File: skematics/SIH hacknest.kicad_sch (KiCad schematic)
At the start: 20 parts, among them J1 Screw_Terminal_01x02, J10 Conn_2Rows-05Pins, J11 oled 1.3inch, J12 oled 0.96inch, J13 Conn_2Rows-05Pins, J14 Conn_2Rows-05Pins, J2 Screw_Terminal_01x02, J3 MQ137, J4 LOADCELL FLOCK, J5 LOAD CELL FEED, J6 BH1750, J7 Conn_2Rows-05Pins, J8 Conn_2Rows-05Pins, J9 Conn_2Rows-05Pins, SW1 SW_SPDT, U1 DHT22, U2 ESP32-S2-WROVER, U3 HX711, U4 BUCK CONVERTER

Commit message: updated sch
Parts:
- added J15: FLOW SENSOR, symbol Connector:Conn_01x03_Pin
- added J16: COMMON RAIL +VE, symbol Connector_Generic:Conn_2Rows-05Pins
- added J17: COMMON RAIL -VE, symbol Connector_Generic:Conn_2Rows-05Pins
- added J18: max9812 MIC, symbol Connector:Conn_01x03_Pin
- added K1: RELAY GENRAL-1, Relay_THT:Relay_StandexMeder_DIP_LowProfile, symbol Relay:DIPxx-1Axx-12x
- added K2: RELAY GENERAL 2, Relay_THT:Relay_StandexMeder_DIP_LowProfile, symbol Relay:DIPxx-1Axx-12x
- added SW2, SW3, SW4, SW5: SW_Push, symbol Switch:SW_Push
- J10, J8: value Conn_2Rows-05Pins -> COMMON RAIL -VE
- J13: value Conn_2Rows-05Pins -> COMMON SDA
- J14: value Conn_2Rows-05Pins -> COMMON SCA
- J7, J9: value Conn_2Rows-05Pins -> COMMON RAIL +VE
- U2: value ESP32-S2-WROVER -> ESP32-WROVER
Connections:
- net at J11.1 (vcc), J12.1 (vcc): now also J15.1 (Pin_1), J16.5 (Pin_5), J18.1 (Pin_1)
- net at J11.2 (gnd), J12.2 (gnd): now also J15.2 (Pin_2), J17.1 (Pin_1), J18.2 (Pin_2)
- net at J9.2 (Pin_2): now also J4.2 (Pin_2); no longer J4.1 (Pin_1)
- net at J10.5 (Pin_5), U3.5 (AGND): now also U2.30 (IO36), SW5.1
- net at J10.2 (Pin_2): now also J4.1 (Pin_1); no longer J4.2 (Pin_2)
- net at J8.1 (Pin_1): now also J17.2 (Pin_2); no longer J10.3 (Pin_3)
- net at J10.4 (Pin_4), J5.2 (Pin_2): now also SW2.2, SW3.2, SW4.2, SW5.2
- net at U2.15 (IO12): now also J15.3 (Pin_3)
- net at U2.16 (IO13): now also J18.3 (Pin_3)
- net at U2.18 (IO15): now also K1.1, K1.14
- net at U2.19 (IO16): now also K2.1, K2.14
- net at J7.1 (Pin_1): now also J16.1 (Pin_1); no longer U2.2 (3V3)
- net at U2.31 (IO37): now also SW4.1
- net at U2.32 (IO38): now also SW3.1
- net at U2.33 (IO39): now also SW2.1
- new net: J12.4 (sca), J13.3 (Pin_3)
- new net: J16.3 (Pin_3), K1.13, K1.2, K2.6
- new net: J16.4 (Pin_4), U2.2 (3V3)
- new net: J17.3 (Pin_3), K1.6, K2.13, K2.2
- new net: J10.3 (Pin_3), J17.4 (Pin_4)
- new net: J13.1 (Pin_1), U2.24 (IO21)
- new net: J14.1 (Pin_1), U2.39 (IO45)
- new net: K2.7, K2.8
- new net: J11.4 (sca), J13.5 (Pin_5)
- new net: K1.7, K1.8
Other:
- moved on the sheet: J9, U3

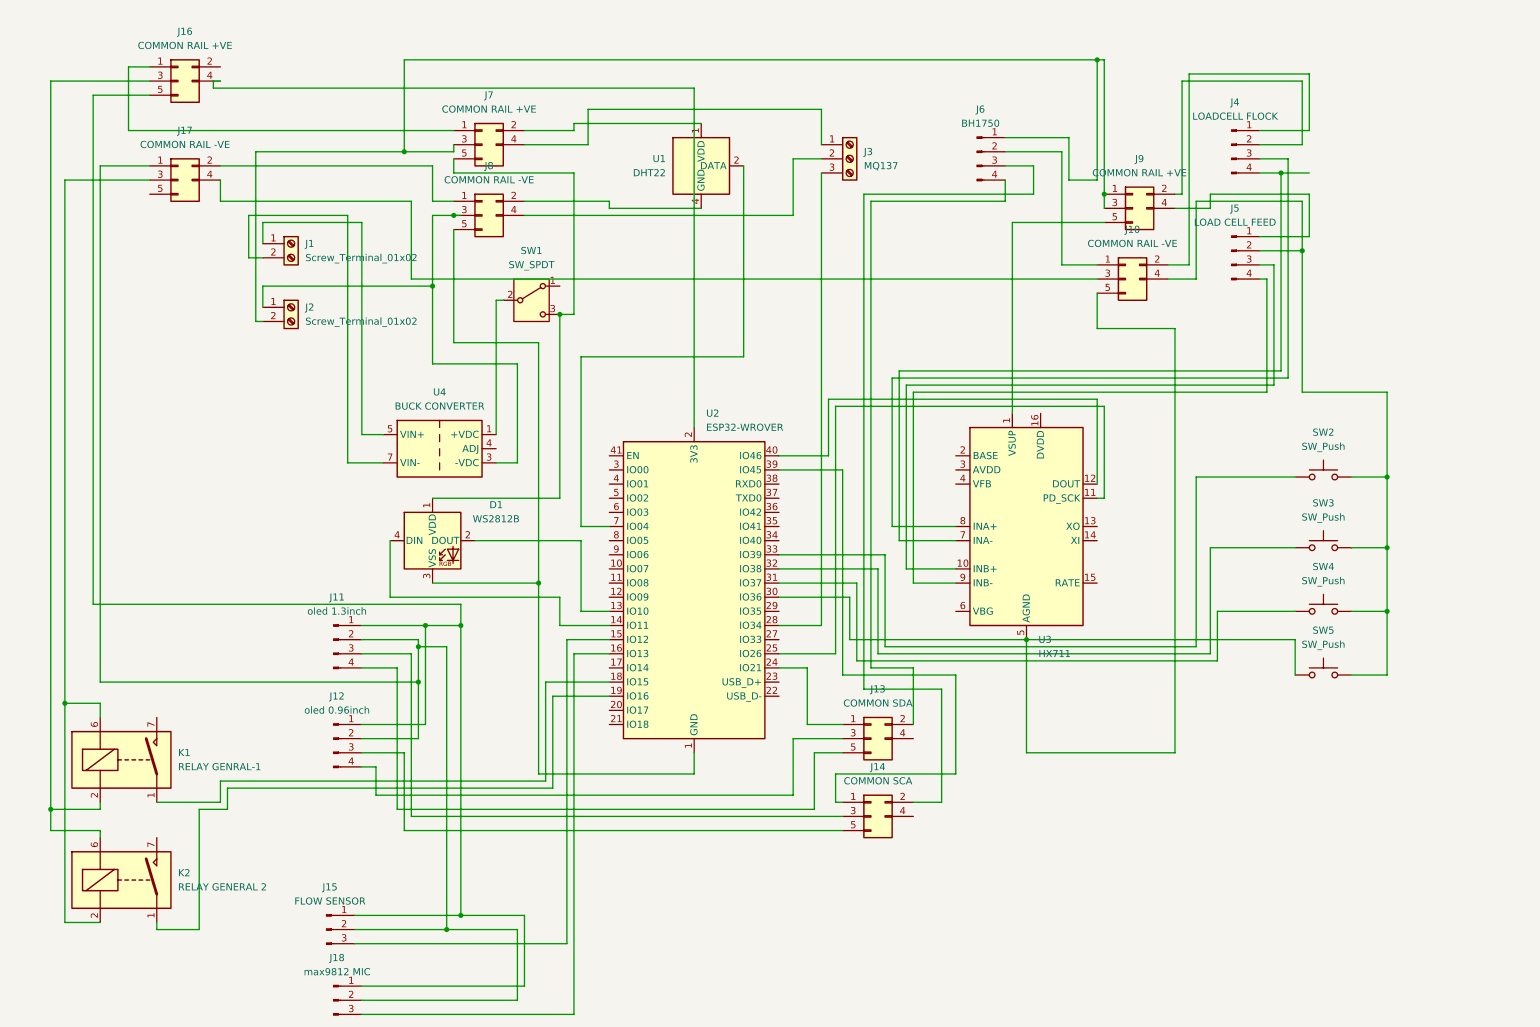
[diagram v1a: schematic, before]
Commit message: Updated Schematics
did the required changes to schematics
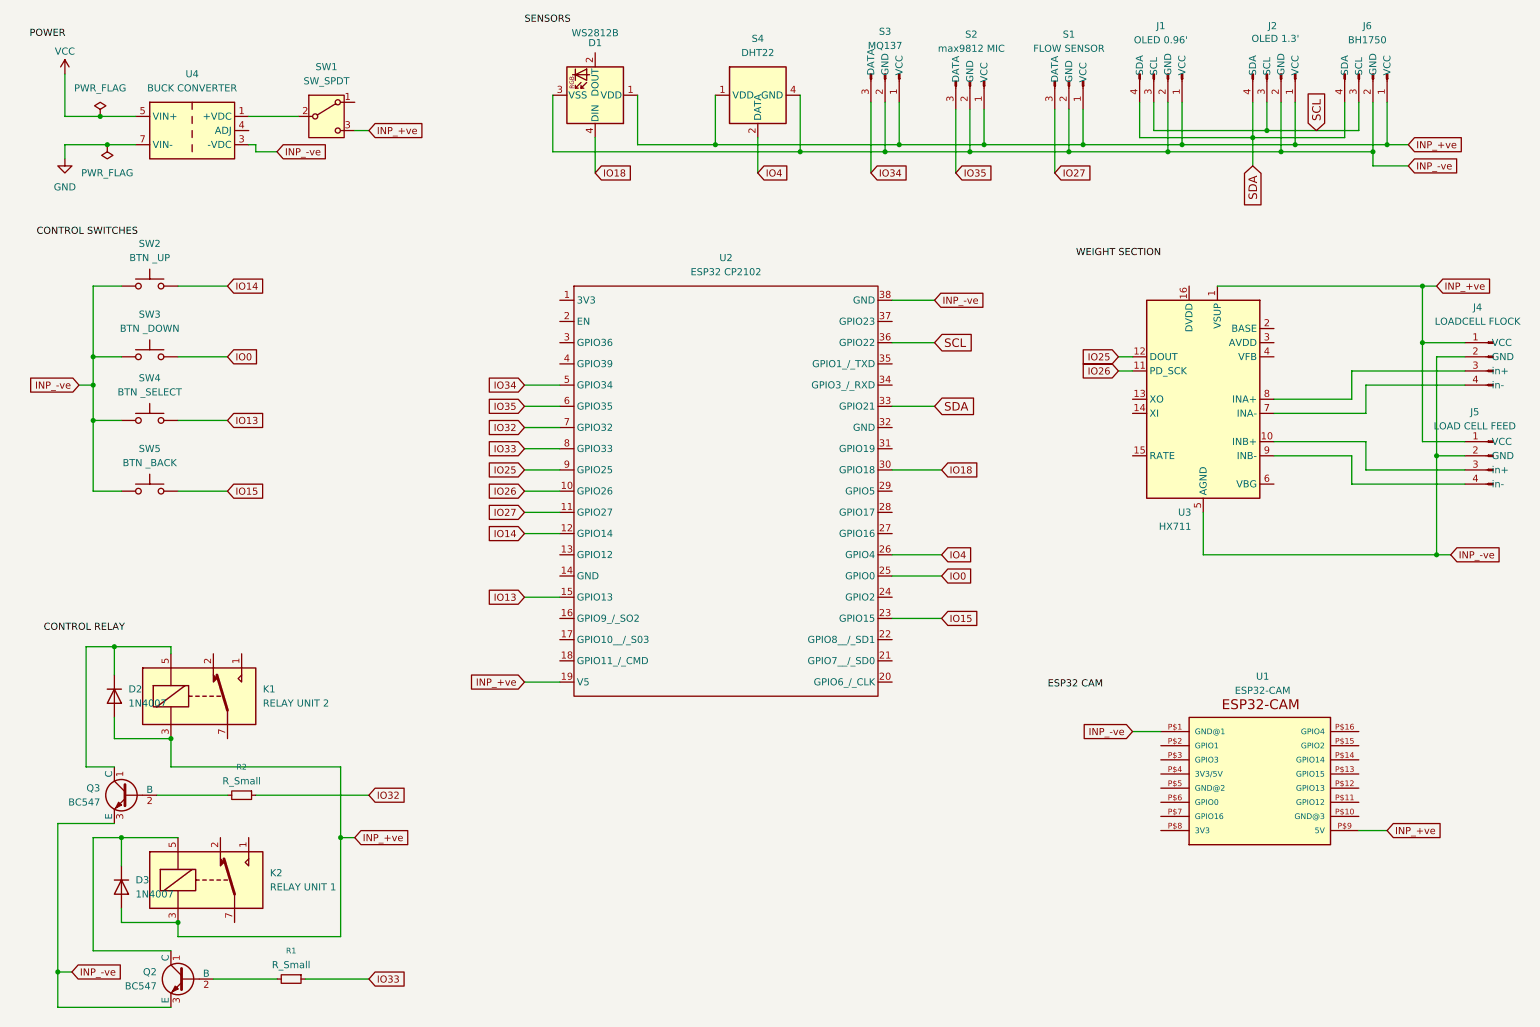
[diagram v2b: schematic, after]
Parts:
- removed J1, J2: Screw_Terminal_01x02, symbol Connector:Screw_Terminal_01x02
- removed J10, J17, J8: COMMON RAIL -VE, symbol Connector_Generic:Conn_2Rows-05Pins
- removed J11: oled 1.3inch, symbol Connector:Conn_01x04_Pin
- removed J12: oled 0.96inch, symbol Connector:Conn_01x04_Pin
- removed J13: COMMON SDA, symbol Connector_Generic:Conn_2Rows-05Pins
- removed J14: COMMON SCA, symbol Connector_Generic:Conn_2Rows-05Pins
- removed J15: FLOW SENSOR, symbol Connector:Conn_01x03_Pin
- removed J16, J7, J9: COMMON RAIL +VE, symbol Connector_Generic:Conn_2Rows-05Pins
- removed J18: max9812 MIC, symbol Connector:Conn_01x03_Pin
- removed J3: MQ137, symbol Connector:Screw_Terminal_01x03
- removed K1: RELAY GENRAL-1, Relay_THT:Relay_StandexMeder_DIP_LowProfile, symbol Relay:DIPxx-1Axx-12x
- removed K2: RELAY GENERAL 2, Relay_THT:Relay_StandexMeder_DIP_LowProfile, symbol Relay:DIPxx-1Axx-12x
- removed U1: DHT22, Sensor:Aosong_DHT11_5.5x12.0_P2.54mm, symbol Sensor:DHT11
- removed U2: ESP32-WROVER, RF_Module:ESP32-S2-WROVER, symbol RF_Module:ESP32-S2-WROVER
- added D2, D3: 1N4007, Diode_THT:D_DO-41_SOD81_P10.16mm_Horizontal, symbol Diode:1N4007
- added J1: OLED 0.96', symbol Connector:Conn_01x04_Pin
- added J2: OLED 1.3', symbol Connector:Conn_01x04_Pin
- added K1: RELAY UNIT 2, Relay_THT:Relay_SPDT_StandexMeder_SIL_Form1C, symbol Relay:SILxx-1Cxx-51x
- added K2: RELAY UNIT 1, Relay_THT:Relay_SPDT_StandexMeder_SIL_Form1C, symbol Relay:SILxx-1Cxx-51x
- added Q2, Q3: BC547, Package_TO_SOT_THT:TO-92_Inline, symbol Transistor_BJT:BC547
- added R1, R2: R_Small, symbol Device:R_Small
- added S1: FLOW SENSOR, symbol Connector:Conn_01x03_Pin
- added S2: max9812 MIC, symbol Connector:Conn_01x03_Pin
- added S3: MQ137, symbol Connector:Conn_01x03_Pin
- added S4: DHT22, Sensor:Aosong_DHT11_5.5x12.0_P2.54mm, symbol Sensor:DHT11
- added U1: ESP32-CAM, ESP32-CAM:ESP32-CAM, symbol ESP32-CAM:ESP32-CAM
- added U2: ESP32 CP2102, Package_SO:ESP32_38Pin, symbol ESP32_38Pin_Symbol:ESP32_38Pin_Symbol
- SW2: value SW_Push -> BTN _UP
- SW3: value SW_Push -> BTN _DOWN
- SW4: value SW_Push -> BTN _SELECT
- SW5: value SW_Push -> BTN _BACK
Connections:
- net INP_-ve: now reaches SW4.1
- net INP_-ve: now also D1.3 (VSS), J4.2 (GND), J5.2 (GND), J6.2 (GND), SW2.1, SW3.1, SW5.1, U3.5 (AGND), U4.3 (-VDC), J1.2 (GND), J2.2 (GND), Q2.3 (E), Q3.3 (E), S1.2 (GND), S2.2 (GND), S3.2 (GND), S4.4 (GND), U1.P$1 (GND@1), U2.38 (GND)
- net INP_+ve: now reaches J6.1 (VCC)
- net INP_+ve: now also D1.1 (VDD), J4.1 (VCC), J5.1 (VCC), SW1.3 (C), U3.1 (VSUP), D2.2 (A), D3.2 (A), J1.1 (VCC), J2.1 (VCC), K1.3, K2.3, S1.1 (VCC), S2.1 (VCC), S3.1 (VCC), S4.1 (VDD), U1.P$9 (5V), U2.19 (V5)
- net IO26: now reaches U3.11 (PD_SCK)
- net IO26: now also U2.10 (GPIO26)
- net IO25: now reaches U3.12 (DOUT)
- net IO25: now also U2.9 (GPIO25)
- net SCL: now reaches J6.3 (SCL)
- net SCL: now also J1.3 (SCL), J2.3 (SCL), U2.36 (GPIO22)
- net SDA: now reaches J6.4 (SDA)
- net SDA: now also J1.4 (SDA), J2.4 (SDA), U2.33 (GPIO21)
- net VCC: now reaches U4.5 (VIN+), U4.6 (VIN+)
- net GND: now reaches U4.7 (VIN-), U4.8 (VIN-)
- net IO18: now reaches D1.4 (DIN)
- net IO18: now also U2.30 (GPIO18)
- new net: D2.1 (K), K1.5, Q3.1 (C)
- new net: Q3.2 (B), R2.2
- new net: Q2.2 (B), R1.2
- new net: D3.1 (K), K2.5, Q2.1 (C)
- new net IO0: SW3.2, U2.25 (GPIO0)
- new net IO13: SW4.2, U2.15 (GPIO13)
- new net IO14: SW2.2, U2.12 (GPIO14)
- new net IO15: SW5.2, U2.23 (GPIO15)
- new net IO27: S1.3 (DATA), U2.11 (GPIO27)
- new net IO32: R2.1, U2.7 (GPIO32)
- new net IO33: R1.1, U2.8 (GPIO33)
- new net IO34: S3.3 (DATA), U2.5 (GPIO34)
- new net IO35: S2.3 (DATA), U2.6 (GPIO35)
- new net IO4: S4.2 (DATA), U2.26 (GPIO4)
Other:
- moved on the sheet: D1, SW1, SW2, SW3, SW4, U3, U4
